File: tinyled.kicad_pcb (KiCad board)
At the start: 2 copper layers, 33.1 x 20.6 mm, 62 parts, among them J1 Conn_01x01_Female, J4 Conn_01x01_Female

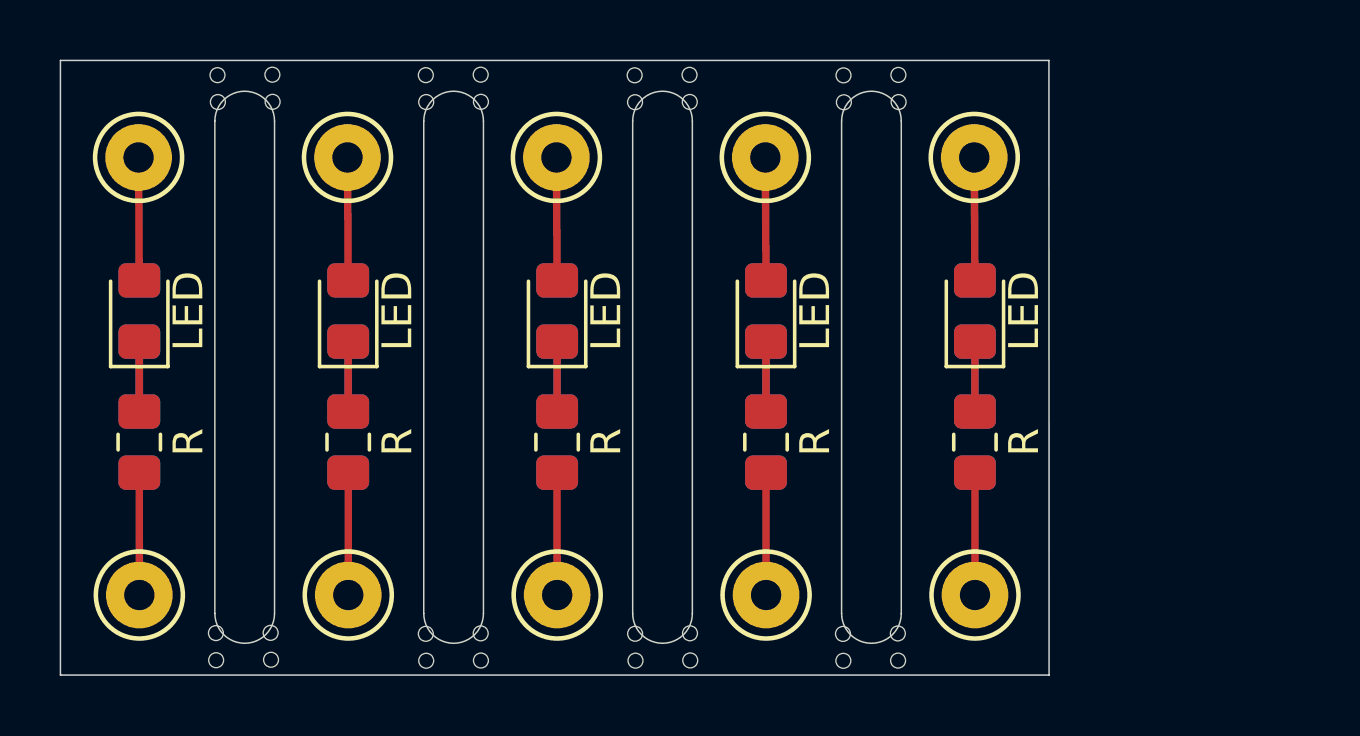
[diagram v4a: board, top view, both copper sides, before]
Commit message: make the strips 3mm wide
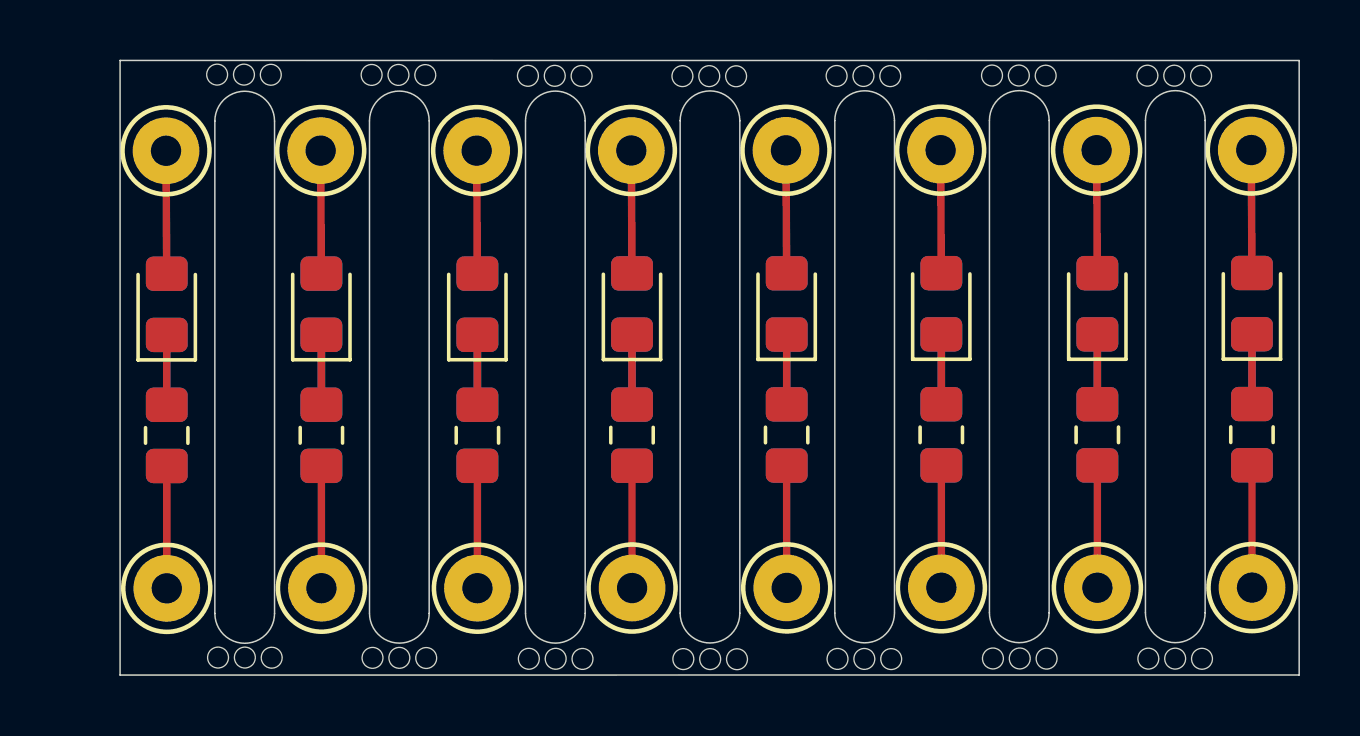
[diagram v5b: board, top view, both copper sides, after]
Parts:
- removed the D1 at (11.8, 84.0) (x2)
- removed the D1 at (-2.19, 84.0)
- removed the D1 at (-9.19, 84.0)
- removed the D1 at (4.81, 84.0)
- removed the D1 at (-9.20, 84.0)
- removed the D1 at (-2.20, 84.0)
- removed the D1 at (4.80, 84.0)
- removed the J1 at (-9.22, 78.9)
- removed the J1 at (-2.22, 78.9)
- removed the J1 at (4.78, 78.9)
- removed the J1 at (11.8, 78.9)
- removed the J4 at (-9.20, 93.5)
- removed the J4 at (-2.20, 93.5)
- removed the J4 at (4.80, 93.5)
- removed the J4 at (11.8, 93.5)
- removed the R1 at (-2.19, 88.4)
- removed the R1 at (11.8, 88.4) (x2)
- removed the R1 at (-9.19, 88.4)
- removed the R1 at (4.81, 88.4)
- removed the R1 at (-9.20, 88.4)
- removed the R1 at (-2.20, 88.4)
- removed the R1 at (4.80, 88.4)
- removed the V at (8.34, 96.9)
- removed the V at (-5.63, 96.9)
- removed the V at (-5.65, 96.0)
- removed the V at (-3.81, 96.0)
- removed the V at (10.2, 78.2)
- removed the V at (8.36, 78.2)
- removed the V at (8.35, 77.3)
- removed the V at (10.2, 77.3)
- removed the V at (1.36, 78.2)
- removed the V at (3.20, 78.2)
- removed the V at (1.35, 77.3)
- removed the V at (8.33, 96.0)
- removed the V at (3.19, 77.3)
- removed the V at (-5.63, 78.2)
- removed the V at (-3.80, 78.2)
- removed the V at (-3.81, 77.3)
- removed the V at (-5.65, 77.3)
- removed the V at (-12.6, 78.2)
- removed the V at (-10.8, 77.3)
- removed the V at (-12.6, 77.3)
- removed the V at (-10.8, 78.2)
- removed the V at (-12.7, 93.6)
- removed the V at (10.2, 96.0)
- removed the V at (-14.6, 94.5)
- removed the V at (-14.6, 93.6)
- removed the V at (10.2, 96.9)
- removed the V at (3.21, 96.0)
- removed the V at (1.37, 96.0)
- removed the V at (1.38, 96.9)
- removed the V at (3.21, 96.9)
- removed the V at (-3.80, 96.9)
- added D1: LED, Diode_SMD:D_0805_2012Metric_Pad1.15x1.40mm_HandSolder, B.Cu at (5.50, 83.8)
- added D1: LED, Diode_SMD:D_0805_2012Metric_Pad1.15x1.40mm_HandSolder, F.Cu at (5.49, 83.8)
- added D1: LED, Diode_SMD:D_0805_2012Metric_Pad1.15x1.40mm_HandSolder, F.Cu at (21.1, 83.8)
- added D1: LED, Diode_SMD:D_0805_2012Metric_Pad1.15x1.40mm_HandSolder, F.Cu at (10.7, 83.8)
- added D1: LED, Diode_SMD:D_0805_2012Metric_Pad1.15x1.40mm_HandSolder, F.Cu at (15.9, 83.8)
- added D1: LED, Diode_SMD:D_0805_2012Metric_Pad1.15x1.40mm_HandSolder, B.Cu at (15.9, 83.8)
- added D1: LED, Diode_SMD:D_0805_2012Metric_Pad1.15x1.40mm_HandSolder, B.Cu at (10.7, 83.8)
- added D1: LED, Diode_SMD:D_0805_2012Metric_Pad1.15x1.40mm_HandSolder, B.Cu at (-10.1, 83.8)
- added D1: LED, Diode_SMD:D_0805_2012Metric_Pad1.15x1.40mm_HandSolder, F.Cu at (-10.1, 83.8)
- added D1: LED, Diode_SMD:D_0805_2012Metric_Pad1.15x1.40mm_HandSolder, B.Cu at (-4.87, 83.8)
- added D1: LED, Diode_SMD:D_0805_2012Metric_Pad1.15x1.40mm_HandSolder, F.Cu at (-4.87, 83.8)
- added D1: LED, Diode_SMD:D_0805_2012Metric_Pad1.15x1.40mm_HandSolder, F.Cu at (0.31, 83.8)
- added D1: LED, Diode_SMD:D_0805_2012Metric_Pad1.15x1.40mm_HandSolder, B.Cu at (0.32, 83.8)
- added D1: LED, Diode_SMD:D_0805_2012Metric_Pad1.15x1.40mm_HandSolder, B.Cu at (21.1, 83.8)
- added J1: Conn_01x01_Female, Wickerlib:CONN-HEADER-STRAIGHT-P2.54MM-1x01, F.Cu at (-10.1, 78.7)
- added J1: Conn_01x01_Female, Wickerlib:CONN-HEADER-STRAIGHT-P2.54MM-1x01, F.Cu at (-4.89, 78.7)
- added J1: Conn_01x01_Female, Wickerlib:CONN-HEADER-STRAIGHT-P2.54MM-1x01, F.Cu at (0.29, 78.7)
- added J1: Conn_01x01_Female, Wickerlib:CONN-HEADER-STRAIGHT-P2.54MM-1x01, F.Cu at (5.47, 78.6)
- added J1: Conn_01x01_Female, Wickerlib:CONN-HEADER-STRAIGHT-P2.54MM-1x01, F.Cu at (15.9, 78.6)
- added J1: Conn_01x01_Female, Wickerlib:CONN-HEADER-STRAIGHT-P2.54MM-1x01, F.Cu at (10.7, 78.6)
- added J1: Conn_01x01_Female, Wickerlib:CONN-HEADER-STRAIGHT-P2.54MM-1x01, F.Cu at (21.1, 78.6)
- added J4: Conn_01x01_Female, Wickerlib:CONN-HEADER-STRAIGHT-P2.54MM-1x01, F.Cu at (-10.1, 93.3)
- added J4: Conn_01x01_Female, Wickerlib:CONN-HEADER-STRAIGHT-P2.54MM-1x01, F.Cu at (0.31, 93.3)
- added J4: Conn_01x01_Female, Wickerlib:CONN-HEADER-STRAIGHT-P2.54MM-1x01, F.Cu at (-4.87, 93.3)
- added J4: Conn_01x01_Female, Wickerlib:CONN-HEADER-STRAIGHT-P2.54MM-1x01, F.Cu at (15.9, 93.3)
- added J4: Conn_01x01_Female, Wickerlib:CONN-HEADER-STRAIGHT-P2.54MM-1x01, F.Cu at (10.7, 93.3)
- added J4: Conn_01x01_Female, Wickerlib:CONN-HEADER-STRAIGHT-P2.54MM-1x01, F.Cu at (5.50, 93.3)
- added J4: Conn_01x01_Female, Wickerlib:CONN-HEADER-STRAIGHT-P2.54MM-1x01, F.Cu at (21.1, 93.3)
- added R1: R, Resistor_SMD:R_0805_2012Metric_Pad1.15x1.40mm_HandSolder, B.Cu at (21.1, 88.2)
- added R1: R, Resistor_SMD:R_0805_2012Metric_Pad1.15x1.40mm_HandSolder, F.Cu at (21.1, 88.2)
- added R1: R, Resistor_SMD:R_0805_2012Metric_Pad1.15x1.40mm_HandSolder, B.Cu at (5.50, 88.2)
- added R1: R, Resistor_SMD:R_0805_2012Metric_Pad1.15x1.40mm_HandSolder, B.Cu at (15.9, 88.2)
- added R1: R, Resistor_SMD:R_0805_2012Metric_Pad1.15x1.40mm_HandSolder, F.Cu at (15.9, 88.2)
- added R1: R, Resistor_SMD:R_0805_2012Metric_Pad1.15x1.40mm_HandSolder, F.Cu at (10.7, 88.2)
- added R1: R, Resistor_SMD:R_0805_2012Metric_Pad1.15x1.40mm_HandSolder, B.Cu at (10.7, 88.2)
- added R1: R, Resistor_SMD:R_0805_2012Metric_Pad1.15x1.40mm_HandSolder, F.Cu at (-10.1, 88.2)
- added R1: R, Resistor_SMD:R_0805_2012Metric_Pad1.15x1.40mm_HandSolder, B.Cu at (-10.1, 88.2)
- added R1: R, Resistor_SMD:R_0805_2012Metric_Pad1.15x1.40mm_HandSolder, F.Cu at (-4.87, 88.2)
- added R1: R, Resistor_SMD:R_0805_2012Metric_Pad1.15x1.40mm_HandSolder, B.Cu at (-4.87, 88.2)
- added R1: R, Resistor_SMD:R_0805_2012Metric_Pad1.15x1.40mm_HandSolder, F.Cu at (0.31, 88.2)
- added R1: R, Resistor_SMD:R_0805_2012Metric_Pad1.15x1.40mm_HandSolder, B.Cu at (0.32, 88.2)
- added R1: R, Resistor_SMD:R_0805_2012Metric_Pad1.15x1.40mm_HandSolder, F.Cu at (5.49, 88.2)
- added V: HOLE-PLATED-200MIL, Wickerlib:HOLE-UNPLATED-200MIL, F.Cu at (12.3, 74.9)
- added V: HOLE-PLATED-200MIL, Wickerlib:HOLE-UNPLATED-200MIL, F.Cu at (-4.12, 75.0)
- added V: HOLE-PLATED-200MIL, Wickerlib:HOLE-UNPLATED-200MIL, F.Cu at (6.22, 75.0)
- added V: HOLE-PLATED-200MIL, Wickerlib:HOLE-UNPLATED-200MIL, F.Cu at (-2.33, 75.0)
- added V: HOLE-PLATED-200MIL, Wickerlib:HOLE-UNPLATED-200MIL, F.Cu at (1.05, 75.0)
- added V: HOLE-PLATED-200MIL, Wickerlib:HOLE-UNPLATED-200MIL, F.Cu at (2.85, 75.0)
- added V: HOLE-PLATED-200MIL, Wickerlib:HOLE-UNPLATED-200MIL, F.Cu at (-13.6, 74.9)
- added V: HOLE-PLATED-200MIL, Wickerlib:HOLE-UNPLATED-200MIL, F.Cu at (-12.7, 74.9)
- added V: HOLE-PLATED-200MIL, Wickerlib:HOLE-UNPLATED-200MIL, F.Cu at (8.02, 75.0)
- added V: HOLE-PLATED-200MIL, Wickerlib:HOLE-UNPLATED-200MIL, F.Cu at (-3.23, 75.0)
- added V: HOLE-PLATED-200MIL, Wickerlib:HOLE-UNPLATED-200MIL, F.Cu at (-14.5, 74.9)
- added V: HOLE-PLATED-200MIL, Wickerlib:HOLE-UNPLATED-200MIL, F.Cu at (-9.36, 74.9)
- added V: HOLE-PLATED-200MIL, Wickerlib:HOLE-UNPLATED-200MIL, F.Cu at (16.6, 74.9)
- added V: HOLE-PLATED-200MIL, Wickerlib:HOLE-UNPLATED-200MIL, F.Cu at (7.12, 75.0)
- added V: HOLE-PLATED-200MIL, Wickerlib:HOLE-UNPLATED-200MIL, F.Cu at (16.7, 94.5)
- added V: HOLE-PLATED-200MIL, Wickerlib:HOLE-UNPLATED-200MIL, F.Cu at (18.5, 94.5)
- added V: HOLE-PLATED-200MIL, Wickerlib:HOLE-UNPLATED-200MIL, F.Cu at (17.6, 94.5)
- added V: HOLE-PLATED-200MIL, Wickerlib:HOLE-UNPLATED-200MIL, F.Cu at (11.5, 94.5)
- added V: HOLE-PLATED-200MIL, Wickerlib:HOLE-UNPLATED-200MIL, F.Cu at (13.3, 94.5)
- added V: HOLE-PLATED-200MIL, Wickerlib:HOLE-UNPLATED-200MIL, F.Cu at (12.4, 94.5)
- added V: HOLE-PLATED-200MIL, Wickerlib:HOLE-UNPLATED-200MIL, F.Cu at (7.15, 94.5)
- added V: HOLE-PLATED-200MIL, Wickerlib:HOLE-UNPLATED-200MIL, F.Cu at (6.25, 94.5)
- added V: HOLE-PLATED-200MIL, Wickerlib:HOLE-UNPLATED-200MIL, F.Cu at (-7.56, 74.9)
- added V: HOLE-PLATED-200MIL, Wickerlib:HOLE-UNPLATED-200MIL, F.Cu at (8.05, 94.5)
- added V: HOLE-PLATED-200MIL, Wickerlib:HOLE-UNPLATED-200MIL, F.Cu at (1.08, 94.5)
- added V: HOLE-PLATED-200MIL, Wickerlib:HOLE-UNPLATED-200MIL, F.Cu at (2.88, 94.5)
- added V: HOLE-PLATED-200MIL, Wickerlib:HOLE-UNPLATED-200MIL, F.Cu at (1.98, 94.5)
- added V: HOLE-PLATED-200MIL, Wickerlib:HOLE-UNPLATED-200MIL, F.Cu at (-2.30, 94.5)
- added V: HOLE-PLATED-200MIL, Wickerlib:HOLE-UNPLATED-200MIL, F.Cu at (-3.20, 94.5)
- added V: HOLE-PLATED-200MIL, Wickerlib:HOLE-UNPLATED-200MIL, F.Cu at (-4.09, 94.5)
- added V: HOLE-PLATED-200MIL, Wickerlib:HOLE-UNPLATED-200MIL, F.Cu at (-8.43, 94.5)
- added V: HOLE-PLATED-200MIL, Wickerlib:HOLE-UNPLATED-200MIL, F.Cu at (-7.53, 94.5)
- added V: HOLE-PLATED-200MIL, Wickerlib:HOLE-UNPLATED-200MIL, F.Cu at (-9.33, 94.5)
- added V: HOLE-PLATED-200MIL, Wickerlib:HOLE-UNPLATED-200MIL, F.Cu at (17.5, 74.9)
- added V: HOLE-PLATED-200MIL, Wickerlib:HOLE-UNPLATED-200MIL, F.Cu at (-13.6, 94.4)
- added V: HOLE-PLATED-200MIL, Wickerlib:HOLE-UNPLATED-200MIL, F.Cu at (-14.5, 94.4)
- added V: HOLE-PLATED-200MIL, Wickerlib:HOLE-UNPLATED-200MIL, F.Cu at (11.4, 74.9)
- added V: HOLE-PLATED-200MIL, Wickerlib:HOLE-UNPLATED-200MIL, F.Cu at (13.2, 74.9)
- added V: HOLE-PLATED-200MIL, Wickerlib:HOLE-UNPLATED-200MIL, F.Cu at (-8.46, 74.9)
- added V: HOLE-PLATED-200MIL, Wickerlib:HOLE-UNPLATED-200MIL, F.Cu at (1.95, 75.0)
- added V: HOLE-PLATED-200MIL, Wickerlib:HOLE-UNPLATED-200MIL, F.Cu at (18.4, 75.0)
- moved J1 0.95 mm to (-15.3, 78.7)
- moved D1 0.95 mm to (-15.3, 83.8) (x2)
- moved R1 0.95 mm to (-15.3, 88.2) (x2)
- moved J4 0.95 mm to (-15.3, 93.3)
- moved V 0.07 mm to (-12.7, 94.4)
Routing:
- net Net-(D1-Pad1): track 23.4 -> 37.5 mm
- net +3V3: track 20.6 -> 33.0 mm
- net GND: track 20.5 -> 32.8 mm
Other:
- board size 33.1 x 20.6 mm -> 39.5 x 20.6 mm

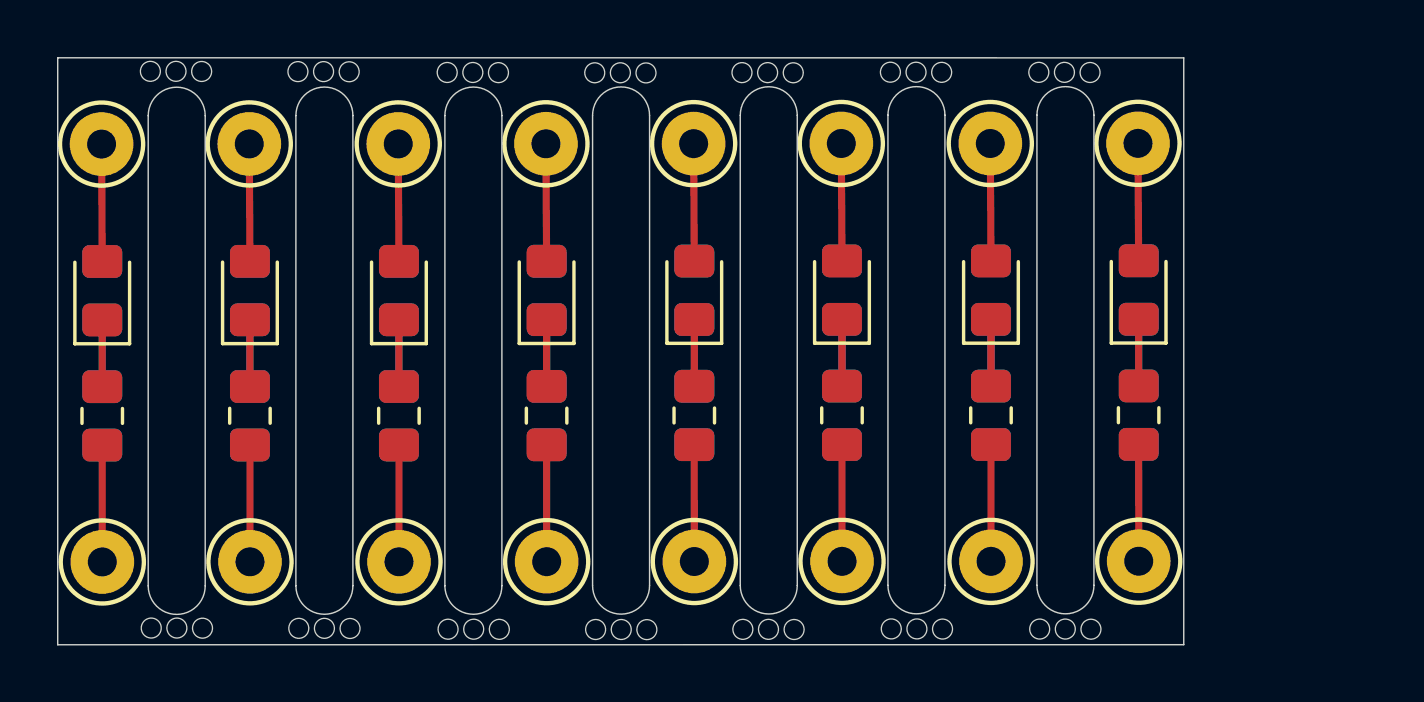
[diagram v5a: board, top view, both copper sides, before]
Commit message: update for 1.9mm width
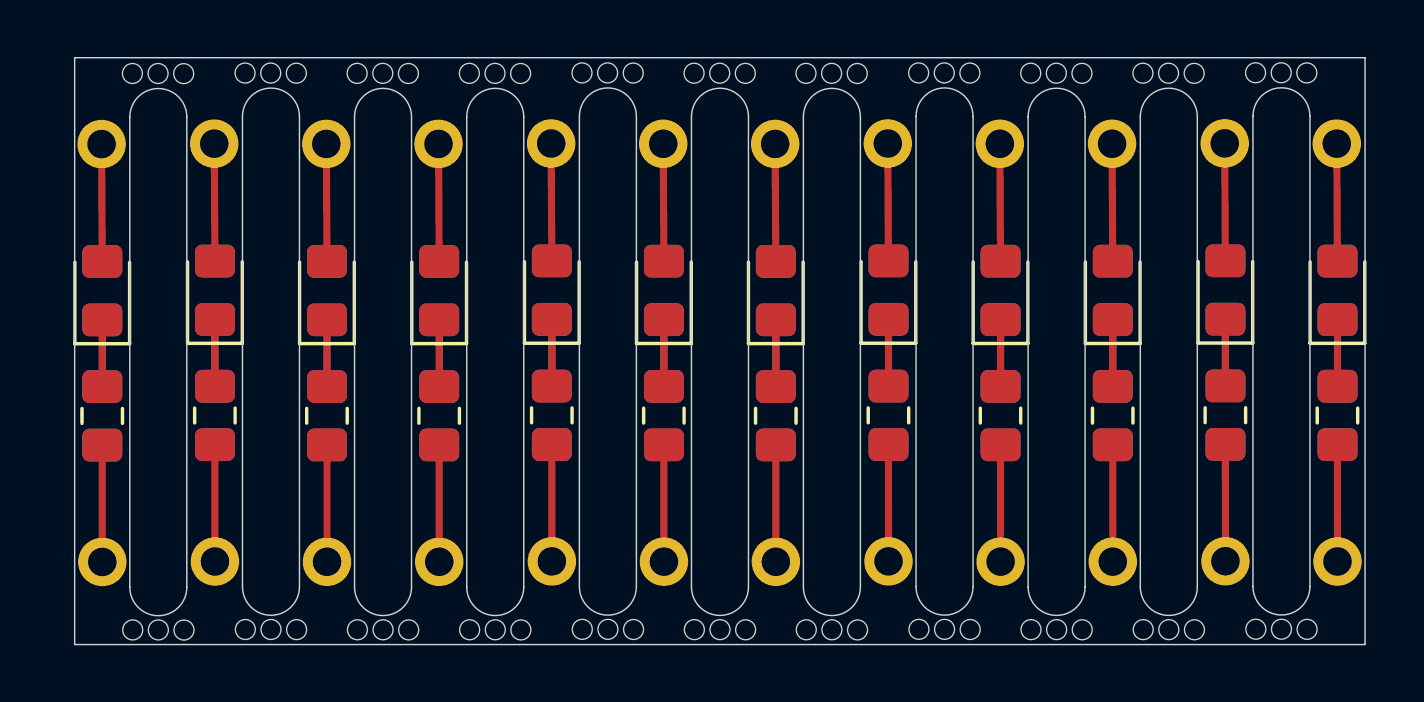
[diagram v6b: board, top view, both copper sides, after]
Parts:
- removed the D1 at (5.50, 83.8)
- removed the D1 at (5.49, 83.8)
- removed the D1 at (21.1, 83.8) (x2)
- removed the D1 at (10.7, 83.8) (x2)
- removed the D1 at (15.9, 83.8) (x2)
- removed the D1 at (-10.1, 83.8) (x2)
- removed the D1 at (-4.87, 83.8) (x2)
- removed the D1 at (0.31, 83.8)
- removed the D1 at (0.32, 83.8)
- removed the J1 at (-10.1, 78.7)
- removed the J1 at (-4.89, 78.7)
- removed the J1 at (0.29, 78.7)
- removed the J1 at (5.47, 78.6)
- removed the J1 at (15.9, 78.6)
- removed the J1 at (10.7, 78.6)
- removed the J1 at (21.1, 78.6)
- removed the J4 at (-10.1, 93.3)
- removed the J4 at (0.31, 93.3)
- removed the J4 at (-4.87, 93.3)
- removed the J4 at (15.9, 93.3)
- removed the J4 at (10.7, 93.3)
- removed the J4 at (5.50, 93.3)
- removed the J4 at (21.1, 93.3)
- removed the R1 at (21.1, 88.2) (x2)
- removed the R1 at (5.50, 88.2)
- removed the R1 at (15.9, 88.2) (x2)
- removed the R1 at (10.7, 88.2) (x2)
- removed the R1 at (-10.1, 88.2) (x2)
- removed the R1 at (-4.87, 88.2) (x2)
- removed the R1 at (0.31, 88.2)
- removed the R1 at (0.32, 88.2)
- removed the R1 at (5.49, 88.2)
- removed the V at (12.3, 74.9)
- removed the V at (-4.12, 75.0)
- removed the V at (6.22, 75.0)
- removed the V at (-2.33, 75.0)
- removed the V at (1.05, 75.0)
- removed the V at (2.85, 75.0)
- removed the V at (-13.6, 74.9)
- removed the V at (-12.7, 74.9)
- removed the V at (8.02, 75.0)
- removed the V at (-3.23, 75.0)
- removed the V at (-14.5, 74.9)
- removed the V at (-9.36, 74.9)
- removed the V at (16.6, 74.9)
- removed the V at (7.12, 75.0)
- removed the V at (16.7, 94.5)
- removed the V at (18.5, 94.5)
- removed the V at (17.6, 94.5)
- removed the V at (11.5, 94.5)
- removed the V at (13.3, 94.5)
- removed the V at (12.4, 94.5)
- removed the V at (7.15, 94.5)
- removed the V at (6.25, 94.5)
- removed the V at (-7.56, 74.9)
- removed the V at (8.05, 94.5)
- removed the V at (1.08, 94.5)
- removed the V at (2.88, 94.5)
- removed the V at (1.98, 94.5)
- removed the V at (-2.30, 94.5)
- removed the V at (-3.20, 94.5)
- removed the V at (-4.09, 94.5)
- removed the V at (-8.43, 94.5)
- removed the V at (-7.53, 94.5)
- removed the V at (-9.33, 94.5)
- removed the V at (17.5, 74.9)
- removed the V at (-13.6, 94.4)
- removed the V at (-14.5, 94.4)
- removed the V at (-12.7, 94.4)
- removed the V at (11.4, 74.9)
- removed the V at (13.2, 74.9)
- removed the V at (-8.46, 74.9)
- removed the V at (1.95, 75.0)
- removed the V at (18.4, 75.0)
- added D1: LED, Diode_SMD:D_0805_2012Metric_Pad1.15x1.40mm_HandSolder, F.Cu at (12.3, 83.8)
- added D1: LED, Diode_SMD:D_0805_2012Metric_Pad1.15x1.40mm_HandSolder, F.Cu at (8.35, 83.8)
- added D1: LED, Diode_SMD:D_0805_2012Metric_Pad1.15x1.40mm_HandSolder, B.Cu at (8.36, 83.8)
- added D1: LED, Diode_SMD:D_0805_2012Metric_Pad1.15x1.40mm_HandSolder, F.Cu at (16.2, 83.8)
- added D1: LED, Diode_SMD:D_0805_2012Metric_Pad1.15x1.40mm_HandSolder, F.Cu at (0.50, 83.8)
- added D1: LED, Diode_SMD:D_0805_2012Metric_Pad1.15x1.40mm_HandSolder, B.Cu at (4.43, 83.8)
- added D1: LED, Diode_SMD:D_0805_2012Metric_Pad1.15x1.40mm_HandSolder, B.Cu at (0.50, 83.8)
- added D1: LED, Diode_SMD:D_0805_2012Metric_Pad1.15x1.40mm_HandSolder, F.Cu at (-3.46, 83.8)
- added D1: LED, Diode_SMD:D_0805_2012Metric_Pad1.15x1.40mm_HandSolder, B.Cu at (-3.45, 83.8)
- added D1: LED, Diode_SMD:D_0805_2012Metric_Pad1.15x1.40mm_HandSolder, F.Cu at (4.43, 83.8)
- added D1: LED, Diode_SMD:D_0805_2012Metric_Pad1.15x1.40mm_HandSolder, F.Cu at (-7.39, 83.8)
- added D1: LED, Diode_SMD:D_0805_2012Metric_Pad1.15x1.40mm_HandSolder, B.Cu at (28.1, 83.8)
- added D1: LED, Diode_SMD:D_0805_2012Metric_Pad1.15x1.40mm_HandSolder, B.Cu at (-7.39, 83.8)
- added D1: LED, Diode_SMD:D_0805_2012Metric_Pad1.15x1.40mm_HandSolder, F.Cu at (-11.3, 83.8)
- added D1: LED, Diode_SMD:D_0805_2012Metric_Pad1.15x1.40mm_HandSolder, B.Cu at (-11.3, 83.8)
- added D1: LED, Diode_SMD:D_0805_2012Metric_Pad1.15x1.40mm_HandSolder, B.Cu at (16.2, 83.8)
- added D1: LED, Diode_SMD:D_0805_2012Metric_Pad1.15x1.40mm_HandSolder, B.Cu at (24.1, 83.8)
- added D1: LED, Diode_SMD:D_0805_2012Metric_Pad1.15x1.40mm_HandSolder, B.Cu at (20.2, 83.8)
- added D1: LED, Diode_SMD:D_0805_2012Metric_Pad1.15x1.40mm_HandSolder, F.Cu at (20.2, 83.8)
- added D1: LED, Diode_SMD:D_0805_2012Metric_Pad1.15x1.40mm_HandSolder, F.Cu at (28.1, 83.8)
- added D1: LED, Diode_SMD:D_0805_2012Metric_Pad1.15x1.40mm_HandSolder, F.Cu at (24.1, 83.8)
- added D1: LED, Diode_SMD:D_0805_2012Metric_Pad1.15x1.40mm_HandSolder, B.Cu at (12.3, 83.8)
- added J1: Conn_01x01_Female, Wickerlib:CONN-HEADER-STRAIGHT-P2.54MM-1x01, F.Cu at (8.33, 78.7)
- added J1: Conn_01x01_Female, Wickerlib:CONN-HEADER-STRAIGHT-P2.54MM-1x01, F.Cu at (-7.42, 78.7)
- added J1: Conn_01x01_Female, Wickerlib:CONN-HEADER-STRAIGHT-P2.54MM-1x01, F.Cu at (-11.3, 78.6)
- added J1: Conn_01x01_Female, Wickerlib:CONN-HEADER-STRAIGHT-P2.54MM-1x01, F.Cu at (16.2, 78.7)
- added J1: Conn_01x01_Female, Wickerlib:CONN-HEADER-STRAIGHT-P2.54MM-1x01, F.Cu at (20.2, 78.7)
- added J1: Conn_01x01_Female, Wickerlib:CONN-HEADER-STRAIGHT-P2.54MM-1x01, F.Cu at (24.1, 78.6)
- added J1: Conn_01x01_Female, Wickerlib:CONN-HEADER-STRAIGHT-P2.54MM-1x01, F.Cu at (12.3, 78.6)
- added J1: Conn_01x01_Female, Wickerlib:CONN-HEADER-STRAIGHT-P2.54MM-1x01, F.Cu at (28.0, 78.6)
- added J1: Conn_01x01_Female, Wickerlib:CONN-HEADER-STRAIGHT-P2.54MM-1x01, F.Cu at (-3.48, 78.7)
- added J1: Conn_01x01_Female, Wickerlib:CONN-HEADER-STRAIGHT-P2.54MM-1x01, F.Cu at (4.40, 78.7)
- added J1: Conn_01x01_Female, Wickerlib:CONN-HEADER-STRAIGHT-P2.54MM-1x01, F.Cu at (0.47, 78.6)
- added J4: Conn_01x01_Female, Wickerlib:CONN-HEADER-STRAIGHT-P2.54MM-1x01, F.Cu at (8.36, 93.3)
- added J4: Conn_01x01_Female, Wickerlib:CONN-HEADER-STRAIGHT-P2.54MM-1x01, F.Cu at (-7.39, 93.3)
- added J4: Conn_01x01_Female, Wickerlib:CONN-HEADER-STRAIGHT-P2.54MM-1x01, F.Cu at (-11.3, 93.3)
- added J4: Conn_01x01_Female, Wickerlib:CONN-HEADER-STRAIGHT-P2.54MM-1x01, F.Cu at (16.2, 93.3)
- added J4: Conn_01x01_Female, Wickerlib:CONN-HEADER-STRAIGHT-P2.54MM-1x01, F.Cu at (20.2, 93.3)
- added J4: Conn_01x01_Female, Wickerlib:CONN-HEADER-STRAIGHT-P2.54MM-1x01, F.Cu at (28.1, 93.3)
- added J4: Conn_01x01_Female, Wickerlib:CONN-HEADER-STRAIGHT-P2.54MM-1x01, F.Cu at (12.3, 93.3)
- added J4: Conn_01x01_Female, Wickerlib:CONN-HEADER-STRAIGHT-P2.54MM-1x01, F.Cu at (24.1, 93.3)
- added J4: Conn_01x01_Female, Wickerlib:CONN-HEADER-STRAIGHT-P2.54MM-1x01, F.Cu at (-3.45, 93.3)
- added J4: Conn_01x01_Female, Wickerlib:CONN-HEADER-STRAIGHT-P2.54MM-1x01, F.Cu at (4.43, 93.3)
- added J4: Conn_01x01_Female, Wickerlib:CONN-HEADER-STRAIGHT-P2.54MM-1x01, F.Cu at (0.50, 93.3)
- added R1: R, Resistor_SMD:R_0805_2012Metric_Pad1.15x1.40mm_HandSolder, F.Cu at (12.3, 88.2)
- added R1: R, Resistor_SMD:R_0805_2012Metric_Pad1.15x1.40mm_HandSolder, B.Cu at (24.1, 88.2)
- added R1: R, Resistor_SMD:R_0805_2012Metric_Pad1.15x1.40mm_HandSolder, B.Cu at (8.36, 88.2)
- added R1: R, Resistor_SMD:R_0805_2012Metric_Pad1.15x1.40mm_HandSolder, F.Cu at (20.2, 88.2)
- added R1: R, Resistor_SMD:R_0805_2012Metric_Pad1.15x1.40mm_HandSolder, F.Cu at (0.50, 88.2)
- added R1: R, Resistor_SMD:R_0805_2012Metric_Pad1.15x1.40mm_HandSolder, F.Cu at (4.43, 88.2)
- added R1: R, Resistor_SMD:R_0805_2012Metric_Pad1.15x1.40mm_HandSolder, B.Cu at (0.50, 88.2)
- added R1: R, Resistor_SMD:R_0805_2012Metric_Pad1.15x1.40mm_HandSolder, B.Cu at (4.43, 88.2)
- added R1: R, Resistor_SMD:R_0805_2012Metric_Pad1.15x1.40mm_HandSolder, F.Cu at (-3.46, 88.2)
- added R1: R, Resistor_SMD:R_0805_2012Metric_Pad1.15x1.40mm_HandSolder, B.Cu at (-3.45, 88.2)
- added R1: R, Resistor_SMD:R_0805_2012Metric_Pad1.15x1.40mm_HandSolder, F.Cu at (-7.39, 88.2)
- added R1: R, Resistor_SMD:R_0805_2012Metric_Pad1.15x1.40mm_HandSolder, F.Cu at (24.1, 88.2)
- added R1: R, Resistor_SMD:R_0805_2012Metric_Pad1.15x1.40mm_HandSolder, B.Cu at (-7.39, 88.2)
- added R1: R, Resistor_SMD:R_0805_2012Metric_Pad1.15x1.40mm_HandSolder, F.Cu at (-11.3, 88.2)
- added R1: R, Resistor_SMD:R_0805_2012Metric_Pad1.15x1.40mm_HandSolder, B.Cu at (-11.3, 88.2)
- added R1: R, Resistor_SMD:R_0805_2012Metric_Pad1.15x1.40mm_HandSolder, F.Cu at (16.2, 88.2)
- added R1: R, Resistor_SMD:R_0805_2012Metric_Pad1.15x1.40mm_HandSolder, B.Cu at (12.3, 88.2)
- added R1: R, Resistor_SMD:R_0805_2012Metric_Pad1.15x1.40mm_HandSolder, B.Cu at (20.2, 88.2)
- added R1: R, Resistor_SMD:R_0805_2012Metric_Pad1.15x1.40mm_HandSolder, B.Cu at (16.2, 88.2)
- added R1: R, Resistor_SMD:R_0805_2012Metric_Pad1.15x1.40mm_HandSolder, F.Cu at (8.35, 88.2)
- added R1: R, Resistor_SMD:R_0805_2012Metric_Pad1.15x1.40mm_HandSolder, B.Cu at (28.1, 88.2)
- added R1: R, Resistor_SMD:R_0805_2012Metric_Pad1.15x1.40mm_HandSolder, F.Cu at (28.1, 88.2)
- added V: HOLE-PLATED-200MIL, Wickerlib:HOLE-UNPLATED-200MIL, F.Cu at (13.3, 94.5)
- added V: HOLE-PLATED-200MIL, Wickerlib:HOLE-UNPLATED-200MIL, F.Cu at (20.3, 75.0)
- added V: HOLE-PLATED-200MIL, Wickerlib:HOLE-UNPLATED-200MIL, F.Cu at (22.1, 94.5)
- added V: HOLE-PLATED-200MIL, Wickerlib:HOLE-UNPLATED-200MIL, F.Cu at (24.2, 75.0)
- added V: HOLE-PLATED-200MIL, Wickerlib:HOLE-UNPLATED-200MIL, F.Cu at (13.3, 75.0)
- added V: HOLE-PLATED-200MIL, Wickerlib:HOLE-UNPLATED-200MIL, F.Cu at (18.1, 75.0)
- added V: HOLE-PLATED-200MIL, Wickerlib:HOLE-UNPLATED-200MIL, F.Cu at (8.46, 75.0)
- added V: HOLE-PLATED-200MIL, Wickerlib:HOLE-UNPLATED-200MIL, F.Cu at (20.3, 94.5)
- added V: HOLE-PLATED-200MIL, Wickerlib:HOLE-UNPLATED-200MIL, F.Cu at (16.4, 94.5)
- added V: HOLE-PLATED-200MIL, Wickerlib:HOLE-UNPLATED-200MIL, F.Cu at (14.2, 94.5)
- added V: HOLE-PLATED-200MIL, Wickerlib:HOLE-UNPLATED-200MIL, F.Cu at (25.1, 75.0)
- added V: HOLE-PLATED-200MIL, Wickerlib:HOLE-UNPLATED-200MIL, F.Cu at (26.0, 94.5)
- added V: HOLE-PLATED-200MIL, Wickerlib:HOLE-UNPLATED-200MIL, F.Cu at (26.0, 75.0)
- added V: HOLE-PLATED-200MIL, Wickerlib:HOLE-UNPLATED-200MIL, F.Cu at (21.2, 75.0)
- added V: HOLE-PLATED-200MIL, Wickerlib:HOLE-UNPLATED-200MIL, F.Cu at (17.2, 75.0)
- added V: HOLE-PLATED-200MIL, Wickerlib:HOLE-UNPLATED-200MIL, F.Cu at (16.3, 75.0)
- added V: HOLE-PLATED-200MIL, Wickerlib:HOLE-UNPLATED-200MIL, F.Cu at (22.1, 75.0)
- added V: HOLE-PLATED-200MIL, Wickerlib:HOLE-UNPLATED-200MIL, F.Cu at (10.3, 94.5)
- added V: HOLE-PLATED-200MIL, Wickerlib:HOLE-UNPLATED-200MIL, F.Cu at (8.47, 94.5)
- added V: HOLE-PLATED-200MIL, Wickerlib:HOLE-UNPLATED-200MIL, F.Cu at (9.37, 94.5)
- added V: HOLE-PLATED-200MIL, Wickerlib:HOLE-UNPLATED-200MIL, F.Cu at (17.3, 94.5)
- added V: HOLE-PLATED-200MIL, Wickerlib:HOLE-UNPLATED-200MIL, F.Cu at (10.3, 75.0)
- added V: HOLE-PLATED-200MIL, Wickerlib:HOLE-UNPLATED-200MIL, F.Cu at (12.4, 94.5)
- added V: HOLE-PLATED-200MIL, Wickerlib:HOLE-UNPLATED-200MIL, F.Cu at (18.2, 94.5)
- added V: HOLE-PLATED-200MIL, Wickerlib:HOLE-UNPLATED-200MIL, F.Cu at (1.51, 94.5)
- added V: HOLE-PLATED-200MIL, Wickerlib:HOLE-UNPLATED-200MIL, F.Cu at (0.61, 94.5)
- added V: HOLE-PLATED-200MIL, Wickerlib:HOLE-UNPLATED-200MIL, F.Cu at (2.40, 75.0)
- added V: HOLE-PLATED-200MIL, Wickerlib:HOLE-UNPLATED-200MIL, F.Cu at (0.60, 75.0)
- added V: HOLE-PLATED-200MIL, Wickerlib:HOLE-UNPLATED-200MIL, F.Cu at (-2.45, 75.0)
- added V: HOLE-PLATED-200MIL, Wickerlib:HOLE-UNPLATED-200MIL, F.Cu at (1.50, 75.0)
- added V: HOLE-PLATED-200MIL, Wickerlib:HOLE-UNPLATED-200MIL, F.Cu at (6.33, 75.0)
- added V: HOLE-PLATED-200MIL, Wickerlib:HOLE-UNPLATED-200MIL, F.Cu at (-3.35, 75.0)
- added V: HOLE-PLATED-200MIL, Wickerlib:HOLE-UNPLATED-200MIL, F.Cu at (4.55, 94.5)
- added V: HOLE-PLATED-200MIL, Wickerlib:HOLE-UNPLATED-200MIL, F.Cu at (14.2, 75.0)
- added V: HOLE-PLATED-200MIL, Wickerlib:HOLE-UNPLATED-200MIL, F.Cu at (2.41, 94.5)
- added V: HOLE-PLATED-200MIL, Wickerlib:HOLE-UNPLATED-200MIL, F.Cu at (5.44, 75.0)
- added V: HOLE-PLATED-200MIL, Wickerlib:HOLE-UNPLATED-200MIL, F.Cu at (4.54, 75.0)
- added V: HOLE-PLATED-200MIL, Wickerlib:HOLE-UNPLATED-200MIL, F.Cu at (-1.54, 94.5)
- added V: HOLE-PLATED-200MIL, Wickerlib:HOLE-UNPLATED-200MIL, F.Cu at (-3.34, 94.5)
- added V: HOLE-PLATED-200MIL, Wickerlib:HOLE-UNPLATED-200MIL, F.Cu at (-2.44, 94.5)
- added V: HOLE-PLATED-200MIL, Wickerlib:HOLE-UNPLATED-200MIL, F.Cu at (5.45, 94.5)
- added V: HOLE-PLATED-200MIL, Wickerlib:HOLE-UNPLATED-200MIL, F.Cu at (-1.55, 75.0)
- added V: HOLE-PLATED-200MIL, Wickerlib:HOLE-UNPLATED-200MIL, F.Cu at (6.34, 94.5)
- added V: HOLE-PLATED-200MIL, Wickerlib:HOLE-UNPLATED-200MIL, F.Cu at (-6.38, 94.5)
- added V: HOLE-PLATED-200MIL, Wickerlib:HOLE-UNPLATED-200MIL, F.Cu at (25.1, 94.5)
- added V: HOLE-PLATED-200MIL, Wickerlib:HOLE-UNPLATED-200MIL, F.Cu at (-7.27, 94.5)
- added V: HOLE-PLATED-200MIL, Wickerlib:HOLE-UNPLATED-200MIL, F.Cu at (-5.49, 75.0)
- added V: HOLE-PLATED-200MIL, Wickerlib:HOLE-UNPLATED-200MIL, F.Cu at (-7.28, 75.0)
- added V: HOLE-PLATED-200MIL, Wickerlib:HOLE-UNPLATED-200MIL, F.Cu at (-6.39, 75.0)
- added V: HOLE-PLATED-200MIL, Wickerlib:HOLE-UNPLATED-200MIL, F.Cu at (-5.48, 94.5)
- added V: HOLE-PLATED-200MIL, Wickerlib:HOLE-UNPLATED-200MIL, F.Cu at (-10.3, 75.0)
- added V: HOLE-PLATED-200MIL, Wickerlib:HOLE-UNPLATED-200MIL, F.Cu at (-11.2, 75.0)
- added V: HOLE-PLATED-200MIL, Wickerlib:HOLE-UNPLATED-200MIL, F.Cu at (-9.41, 94.5)
- added V: HOLE-PLATED-200MIL, Wickerlib:HOLE-UNPLATED-200MIL, F.Cu at (-11.2, 94.5)
- added V: HOLE-PLATED-200MIL, Wickerlib:HOLE-UNPLATED-200MIL, F.Cu at (-10.3, 94.5)
- added V: HOLE-PLATED-200MIL, Wickerlib:HOLE-UNPLATED-200MIL, F.Cu at (24.2, 94.5)
- added V: HOLE-PLATED-200MIL, Wickerlib:HOLE-UNPLATED-200MIL, F.Cu at (-9.42, 75.0)
- added V: HOLE-PLATED-200MIL, Wickerlib:HOLE-UNPLATED-200MIL, F.Cu at (-13.4, 75.0)
- added V: HOLE-PLATED-200MIL, Wickerlib:HOLE-UNPLATED-200MIL, F.Cu at (-15.2, 75.0)
- added V: HOLE-PLATED-200MIL, Wickerlib:HOLE-UNPLATED-200MIL, F.Cu at (-14.3, 75.0)
- added V: HOLE-PLATED-200MIL, Wickerlib:HOLE-UNPLATED-200MIL, F.Cu at (-13.4, 94.5)
- added V: HOLE-PLATED-200MIL, Wickerlib:HOLE-UNPLATED-200MIL, F.Cu at (-14.3, 94.5)
- added V: HOLE-PLATED-200MIL, Wickerlib:HOLE-UNPLATED-200MIL, F.Cu at (-15.2, 94.5)
- added V: HOLE-PLATED-200MIL, Wickerlib:HOLE-UNPLATED-200MIL, F.Cu at (21.2, 94.5)
- added V: HOLE-PLATED-200MIL, Wickerlib:HOLE-UNPLATED-200MIL, F.Cu at (12.4, 75.0)
- added V: HOLE-PLATED-200MIL, Wickerlib:HOLE-UNPLATED-200MIL, F.Cu at (9.36, 75.0)
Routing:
- net Net-(D1-Pad1): track 37.5 -> 56.2 mm
- net +3V3: track 33.0 -> 49.5 mm
- net GND: track 32.8 -> 49.2 mm
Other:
- board size 39.5 x 20.6 mm -> 45.3 x 20.6 mm
